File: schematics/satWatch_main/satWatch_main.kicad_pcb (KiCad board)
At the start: 4 copper layers, 121 x 41.3 mm, 152 parts, among them J1 2167010509_MOLEX, J10 BAT+, J11 BAT-, J2 Pogo_02x03_UARTPROG, J3 855-22-006-10-001101, J4 UJ20-C-H-G-MSMT-2B-P16-TR, J5 SOLDER POINT, J6 SOLDER POINT, J7 2167010509_MOLEX, J8 MOTOR+, J9 MOTOR-, Q1 DMP1045U, Q2 RE1C002UN, Q3 RE1C002UN, Q4 S8050, Q5 S8050, Q6 MMBT2222A, Q7 FS8205, SW1 R-667995, SW2 R-667995, SW3 EVQ-P7A01P, SW4 EVQ-P7A01P, SW5 EVQ-P7A01P, SW6 EVQ-P7A01P, SW7 EVQ-P7A01P, U1 PAM2401SCADJ, U10 NCP186AMX330TAG, U13 DRV2605LDGS, U14 DW01A, U2 MIC5365-1.8YC5, U3 ESP32-S3-MINI-1, U4 MAX30101EFD_T, U5 BNO085, U6 DS3231MZ, U7 CP2102N-Axx-xQFN28, U8 AMS1117-3.3, U9 TP4056-42-ESOP8, Y1 32.768Hz

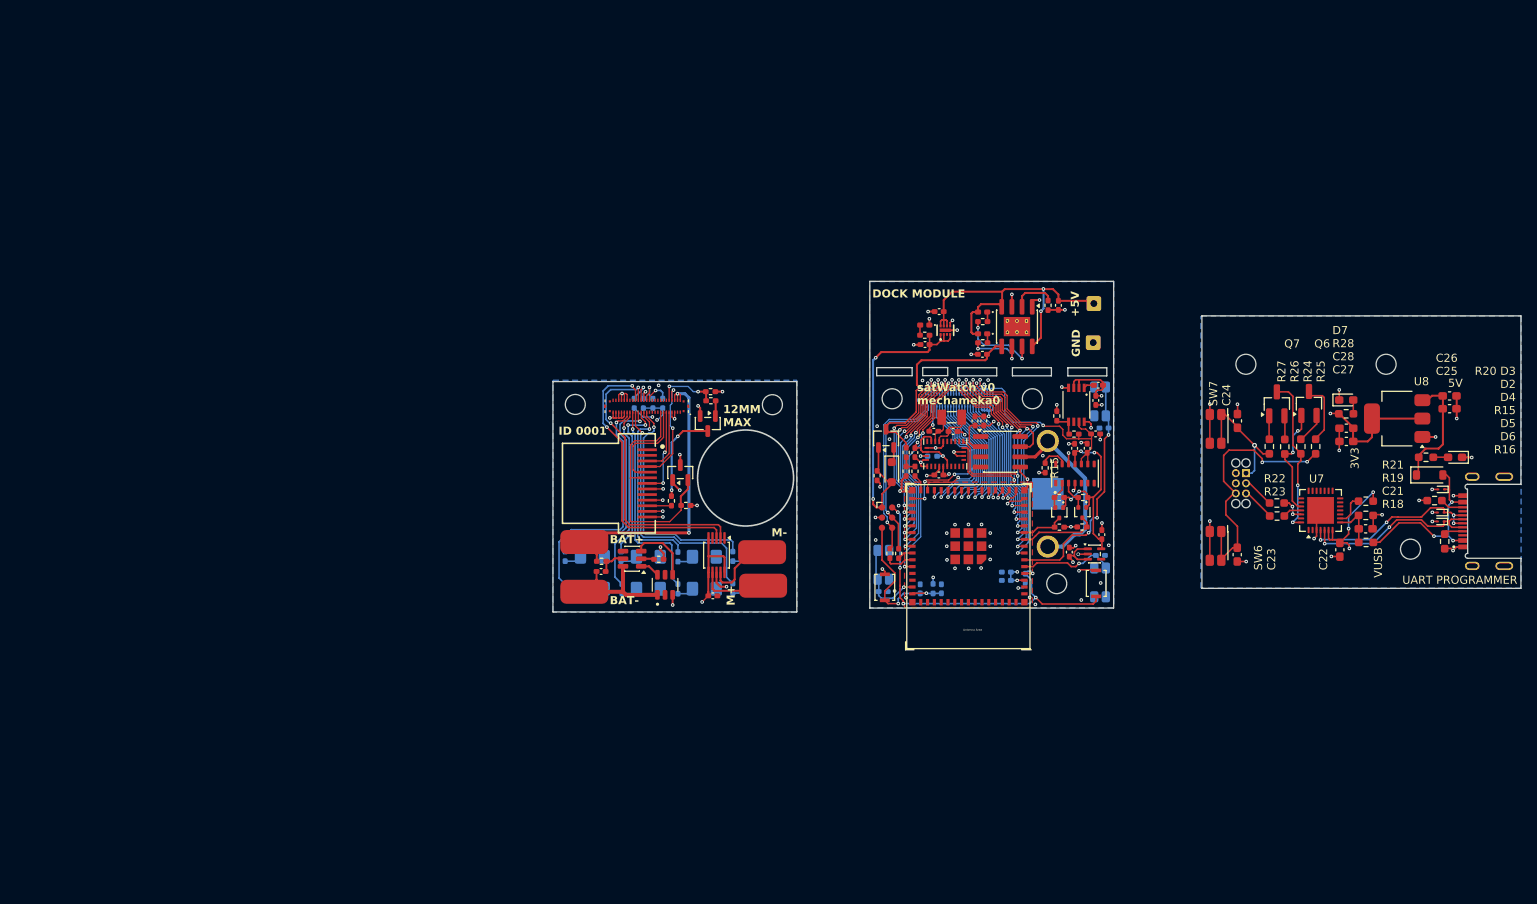
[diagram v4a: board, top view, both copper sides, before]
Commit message: v1.2
WIP of major revisions of PCB board. Changed components and layout for better routing
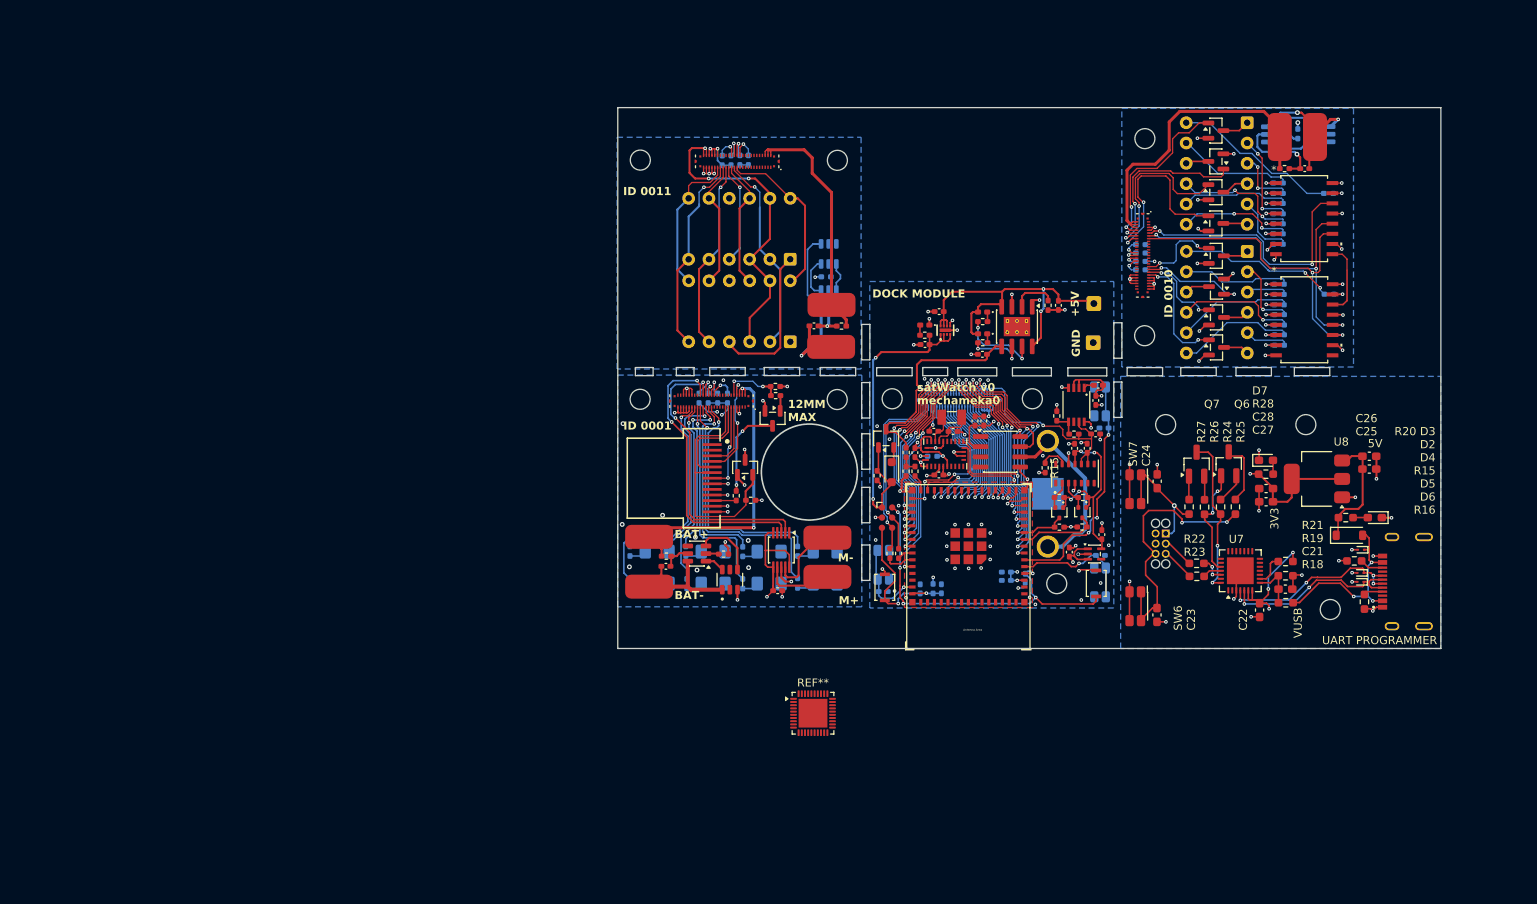
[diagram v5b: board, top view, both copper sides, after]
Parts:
- added C35: 0.1uF, Capacitor_SMD:C_0402_1005Metric_Pad0.74x0.62mm_HandSolder, F.Cu at (181.4, 50.2)
- added C36: 0.1uF, Capacitor_SMD:C_0402_1005Metric_Pad0.74x0.62mm_HandSolder, F.Cu at (120.0, 69.9)
- added DS1: HCMS-2901, Package_DIP:DIP-12_W7.62mm, B.Cu at (117.1, 71.9)
- added DS2: HCMS-2901, Package_DIP:DIP-12_W7.62mm, B.Cu at (117.1, 61.6)
- added H1: MountingHole, MountingHole:MountingHole_2.5mm, F.Cu at (123.0, 49.2)
- added H1: MountingHole, MountingHole:MountingHole_2.5mm, F.Cu at (161.4, 46.5)
- added H2: MountingHole, MountingHole:MountingHole_2.5mm, F.Cu at (161.4, 71.1)
- added H2: MountingHole, MountingHole:MountingHole_2.5mm, F.Cu at (98.3, 49.2)
- added J12: BAT+, Connector_Wire:SolderWirePad_1x01_SMD_3x6mm, F.Cu at (178.2, 46.3)
- added J13: BAT-, Connector_Wire:SolderWirePad_1x01_SMD_3x6mm, F.Cu at (182.7, 46.3)
- added J14: 2167010509_MOLEX, footprint:CON_2167010509_MOL, F.Cu at (161.1, 61.1)
- added J15: BAT+, Connector_Wire:SolderWirePad_1x01_SMD_3x6mm, F.Cu at (122.2, 67.3)
- added J16: BAT-, Connector_Wire:SolderWirePad_1x01_SMD_3x6mm, F.Cu at (122.2, 72.5)
- added J17: 2167010509_MOLEX, footprint:CON_2167010509_MOL, F.Cu at (110.4, 49.3)
- added Q10: MMBT2222ALT3G, Package_TO_SOT_SMD:SOT-23, F.Cu at (170.3, 49.3)
- added Q11: MMBT2222ALT3G, Package_TO_SOT_SMD:SOT-23, F.Cu at (170.3, 53.2)
- added Q12: MMBT2222ALT3G, Package_TO_SOT_SMD:SOT-23, F.Cu at (170.3, 57.1)
- added Q13: MMBT2222ALT3G, Package_TO_SOT_SMD:SOT-23, F.Cu at (170.3, 61.1)
- added Q14: MMBT2222ALT3G, Package_TO_SOT_SMD:SOT-23, F.Cu at (170.3, 65.0)
- added Q15: MMBT2222ALT3G, Package_TO_SOT_SMD:SOT-23, F.Cu at (170.3, 68.8)
- added Q16: MMBT2222ALT3G, Package_TO_SOT_SMD:SOT-23, F.Cu at (170.3, 72.6)
- added Q17: FS8205, footprint:SOT95P280X145-6N, B.Cu at (121.9, 60.9)
- added Q8: FS8205, footprint:SOT95P280X145-6N, B.Cu at (183.4, 45.9)
- added Q9: MMBT2222ALT3G, Package_TO_SOT_SMD:SOT-23, F.Cu at (170.3, 45.5)
- added R51: 100, Resistor_SMD:R_0402_1005Metric_Pad0.72x0.64mm_HandSolder, F.Cu at (178.8, 50.2)
- added R52: 1K, Resistor_SMD:R_0402_1005Metric_Pad0.72x0.64mm_HandSolder, B.Cu at (180.5, 45.9)
- added R53: 10K, Resistor_SMD:R_0402_1005Metric_Pad0.72x0.64mm_HandSolder, B.Cu at (160.8, 59.7)
- added R54: 10K, Resistor_SMD:R_0402_1005Metric_Pad0.72x0.64mm_HandSolder, B.Cu at (160.8, 60.8)
- added R55: 10K, Resistor_SMD:R_0402_1005Metric_Pad0.72x0.64mm_HandSolder, B.Cu at (160.8, 61.8)
- added R56: 10K, Resistor_SMD:R_0402_1005Metric_Pad0.72x0.64mm_HandSolder, B.Cu at (160.8, 62.9)
- added R57: 360, Resistor_SMD:R_0402_1005Metric_Pad0.72x0.64mm_HandSolder, B.Cu at (184.3, 53.3)
- added R58: 360, Resistor_SMD:R_0402_1005Metric_Pad0.72x0.64mm_HandSolder, B.Cu at (178.1, 52.0)
- added R59: 360, Resistor_SMD:R_0402_1005Metric_Pad0.72x0.64mm_HandSolder, B.Cu at (178.1, 53.3)
- added R60: 360, Resistor_SMD:R_0402_1005Metric_Pad0.72x0.64mm_HandSolder, B.Cu at (178.0, 54.6)
- added R61: 360, Resistor_SMD:R_0402_1005Metric_Pad0.72x0.64mm_HandSolder, B.Cu at (178.1, 55.9)
- added R62: 360, Resistor_SMD:R_0402_1005Metric_Pad0.72x0.64mm_HandSolder, B.Cu at (178.1, 57.1)
- added R63: 360, Resistor_SMD:R_0402_1005Metric_Pad0.72x0.64mm_HandSolder, B.Cu at (178.0, 58.4)
- added R64: 360, Resistor_SMD:R_0402_1005Metric_Pad0.72x0.64mm_HandSolder, B.Cu at (178.0, 59.7)
- added R65: 360, Resistor_SMD:R_0402_1005Metric_Pad0.72x0.64mm_HandSolder, B.Cu at (184.4, 65.9)
- added R66: 360, Resistor_SMD:R_0402_1005Metric_Pad0.72x0.64mm_HandSolder, B.Cu at (178.2, 64.7)
- added R67: 360, Resistor_SMD:R_0402_1005Metric_Pad0.72x0.64mm_HandSolder, B.Cu at (178.2, 66.0)
- added R68: 360, Resistor_SMD:R_0402_1005Metric_Pad0.72x0.64mm_HandSolder, B.Cu at (178.2, 67.3)
- added R69: 360, Resistor_SMD:R_0402_1005Metric_Pad0.72x0.64mm_HandSolder, B.Cu at (178.2, 68.5)
- added R70: 360, Resistor_SMD:R_0402_1005Metric_Pad0.72x0.64mm_HandSolder, B.Cu at (178.2, 69.8)
- added R71: 360, Resistor_SMD:R_0402_1005Metric_Pad0.72x0.64mm_HandSolder, B.Cu at (178.2, 71.0)
- added R72: 360, Resistor_SMD:R_0402_1005Metric_Pad0.72x0.64mm_HandSolder, B.Cu at (178.2, 72.3)
- added R73: 100, Resistor_SMD:R_0402_1005Metric_Pad0.72x0.64mm_HandSolder, F.Cu at (123.5, 69.9)
- added R74: 10K, Resistor_SMD:R_0402_1005Metric_Pad0.72x0.64mm_HandSolder, B.Cu at (111.8, 49.2)
- added R75: 10K, Resistor_SMD:R_0402_1005Metric_Pad0.72x0.64mm_HandSolder, B.Cu at (110.8, 49.2)
- added R76: 10K, Resistor_SMD:R_0402_1005Metric_Pad0.72x0.64mm_HandSolder, B.Cu at (109.7, 49.2)
- added R77: 10K, Resistor_SMD:R_0402_1005Metric_Pad0.72x0.64mm_HandSolder, B.Cu at (108.6, 49.2)
- added R78: 1K, Resistor_SMD:R_0402_1005Metric_Pad0.72x0.64mm_HandSolder, B.Cu at (121.5, 63.8)
- added REF**: QFN-40-1EP_5x5mm_P0.4mm_EP3.6x3.6mm, Package_DFN_QFN:QFN-40-1EP_5x5mm_P0.4mm_EP3.6x3.6mm, F.Cu at (119.9, 118.3)
- added U15: DW01A, Package_TO_SOT_SMD:SOT-23-6, B.Cu at (177.7, 46.0)
- added U16: ~, Package_DIP:DIP-12_W7.62mm, B.Cu at (174.2, 44.5)
- added U17: SN74HC595NSR, footprint:NS16-L, F.Cu at (181.3, 56.5)
- added U18: SN74HC595NSR, footprint:NS16-L, F.Cu at (181.3, 69.1)
- added U19: ~, Package_DIP:DIP-12_W7.62mm, B.Cu at (174.2, 60.6)
- added U20: DW01A, Package_TO_SOT_SMD:SOT-23-6, B.Cu at (121.9, 66.6)
- Q6: value MMBT2222A -> MMBT2222ALT3G
- moved C25 12.6 mm to (179.0, 102.8)
- moved D5 12.6 mm to (188.3, 101.9)
- moved H1 12.6 mm to (181.5, 82.2)
- moved H2 12.6 mm to (164.0, 82.2)
- moved J3 12.6 mm to (163.4, 97.1)
- moved J4 12.6 mm to (195.1, 101.9)
- moved Q4 12.6 mm to (171.9, 87.1)
- moved Q5 12.6 mm to (167.9, 87.2)
- moved R17 12.6 mm to (188.8, 104.4)
- moved R18 12.6 mm to (176.5, 88.4)
- moved R21 12.6 mm to (179.0, 101.1)
- moved R23 12.6 mm to (170.8, 92.5)
- moved R25 12.6 mm to (167.9, 99.6)
- moved R26 12.6 mm to (167.9, 101.2)
- moved R27 12.6 mm to (172.7, 92.5)
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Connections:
- J7 pad 49: FRONT_5V -> unconnected-(J7-Pin_49-Pad49)
- J7 pad 50: FRONT_5V -> unconnected-(J7-Pin_50-Pad50)
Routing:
- net /face2/GPIO34: track 0.00 -> 42.2 mm, vias 0 -> 3
- net /face2/GPIO33: track 0.00 -> 42.0 mm, vias 0 -> 2
- net /face2/BAT+: track 0.00 -> 39.8 mm
- net FRONT_5V: track 0.00 -> 39.6 mm, vias 0 -> 3
- net /face2/GPIO35: track 0.00 -> 33.0 mm, vias 0 -> 2
- net FRONT_GND: track 24.1 -> 55.6 mm, vias 11 -> 39
- net /face3/BAT+: track 0.00 -> 31.3 mm
- net Net-(J16-Pin_1): track 0.00 -> 26.8 mm, vias 0 -> 1
- net /face3/CLK: track 0.00 -> 25.0 mm, vias 0 -> 1
- net /face3/GPIO17: track 0.00 -> 25.0 mm, vias 0 -> 1
- net /face3/GPIO14: track 0.00 -> 23.7 mm, vias 0 -> 1
- net /face2/CAT1_4: track 0.00 -> 23.6 mm, vias 0 -> 2
- net FRONT_3V3: track 26.7 -> 49.4 mm, vias 8 -> 16
- net /face2/CAT1_1: track 0.00 -> 21.8 mm, vias 0 -> 2
- net /face2/CAT1_3: track 0.00 -> 21.7 mm, vias 0 -> 2
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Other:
- board size 121 x 41.3 mm -> 102.9 x 67.6 mm
- board text added: "HCMS-2901 TOP->BOTTOM DATA"
- board text added: "HP BUBBLE 1->2"
- board text added: "ID 0010"
- board text added: "ID 0011"
- board text added: "WATCHFACE 1"
